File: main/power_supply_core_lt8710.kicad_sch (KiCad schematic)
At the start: 31 parts, among them Q601 IXTP28P065T, Q602 TK4R3E06PL, U601 LT8710

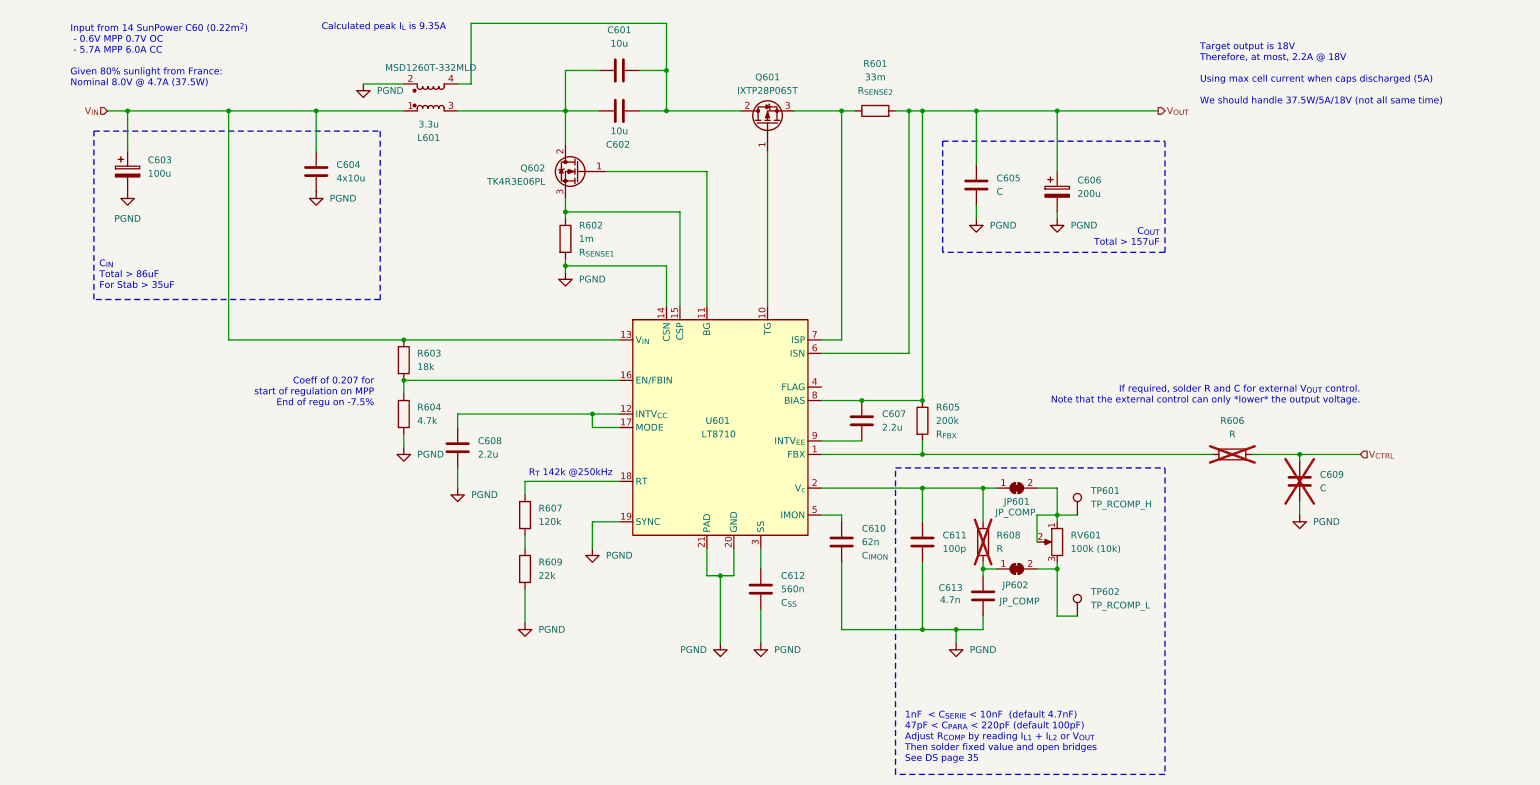
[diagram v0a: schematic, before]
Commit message: Finalize sch and start component mapping
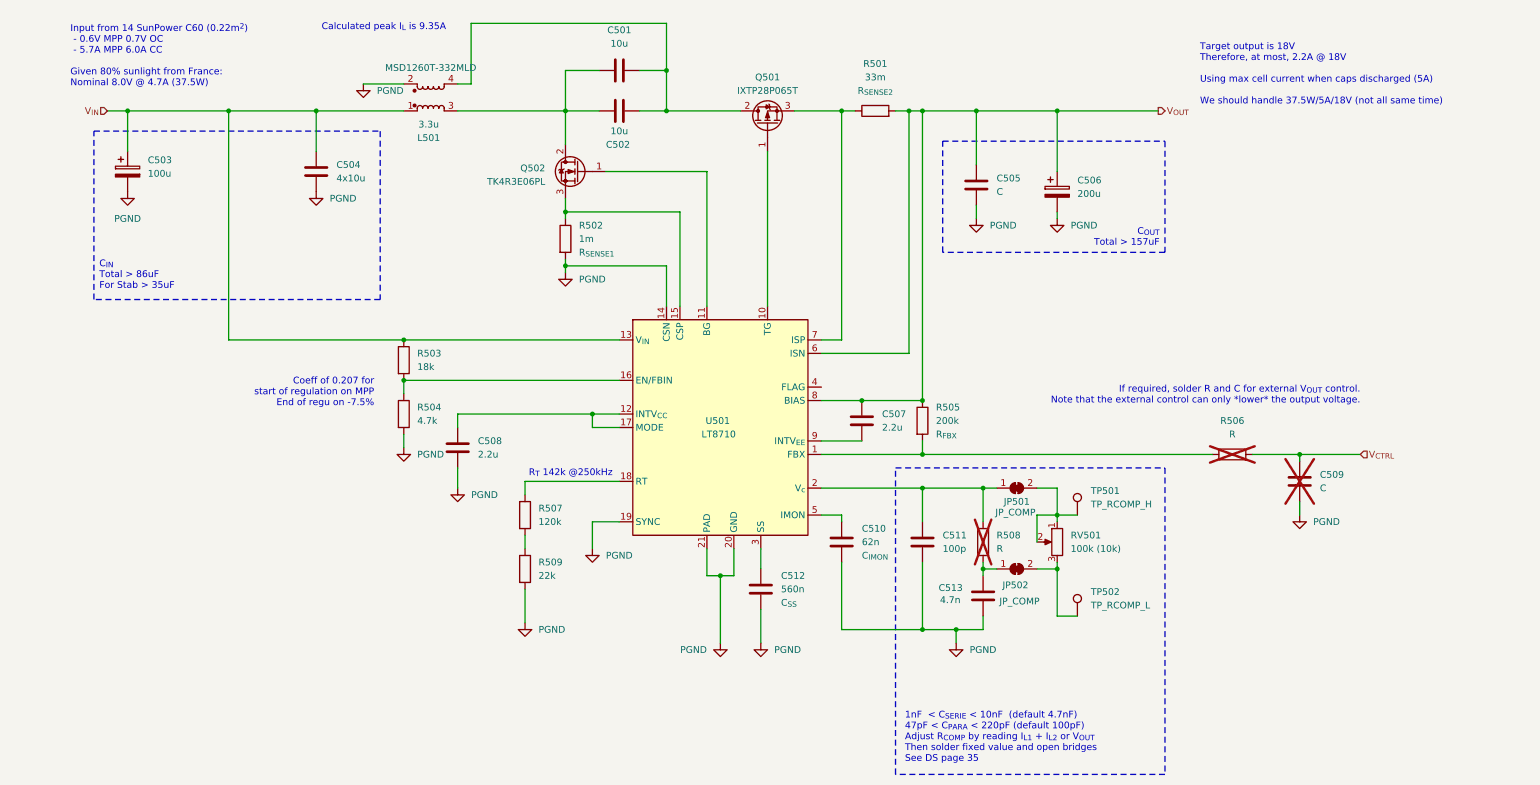
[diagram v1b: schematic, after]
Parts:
- C501: renamed from C601; footprint (none) -> Capacitor_SMD:C_0805_2012Metric
- C502: renamed from C602; footprint (none) -> Capacitor_SMD:C_0805_2012Metric
- C503: renamed from C603; footprint (none) -> Capacitor_SMD:C_0805_2012Metric
- C507: renamed from C607; footprint (none) -> Capacitor_SMD:C_0805_2012Metric
- C508: renamed from C608; footprint (none) -> Capacitor_SMD:C_0805_2012Metric
- C510: renamed from C610; footprint (none) -> Capacitor_SMD:C_0805_2012Metric
- C511: renamed from C611; footprint (none) -> Capacitor_SMD:C_0805_2012Metric
- C512: renamed from C612; footprint (none) -> Capacitor_SMD:C_0805_2012Metric
- C513: renamed from C613; footprint (none) -> Capacitor_SMD:C_0805_2012Metric
- JP501: renamed from JP601; footprint (none) -> Jumper:SolderJumper-2_P1.3mm_Open_TrianglePad1.0x1.5mm
- JP502: renamed from JP602; footprint (none) -> Jumper:SolderJumper-2_P1.3mm_Open_TrianglePad1.0x1.5mm
- Q501: renamed from Q601; footprint (none) -> Package_TO_SOT_THT:TO-220-3_Horizontal_TabUp
- R503: renamed from R603; footprint (none) -> Resistor_SMD:R_0805_2012Metric
- R504: renamed from R604; footprint (none) -> Resistor_SMD:R_0805_2012Metric
- R505: renamed from R605; footprint (none) -> Resistor_SMD:R_0805_2012Metric
- R506: renamed from R606; footprint (none) -> Resistor_SMD:R_0805_2012Metric
- R507: renamed from R607; footprint (none) -> Resistor_SMD:R_0805_2012Metric
- R508: renamed from R608; footprint (none) -> Resistor_SMD:R_0805_2012Metric
- R509: renamed from R609; footprint (none) -> Resistor_SMD:R_0805_2012Metric
- renumbered C604 to C504, C605 to C505, C606 to C506, C609 to C509, L601 to L501, Q602 to Q502, R601 to R501, R602 to R502, RV601 to RV501, TP601 to TP501, TP602 to TP502, U601 to U501

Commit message: update BOM
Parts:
- added C504, C505, C506: 10u, Capacitor_SMD:C_0805_2012Metric, symbol Device:C
- C507: renamed from C504; value 4x10u -> 10u; footprint (none) -> Capacitor_SMD:C_0805_2012Metric
- TP501, TP502: footprint (none) -> TestPoint:TestPoint_Keystone_5010-5014_Multipurpose
- renumbered C505 to C508, C506 to C509, C507 to C510, C508 to C511, C509 to C512, C510 to C513, C511 to C514, C512 to C515, C513 to C516
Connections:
- net PGND: now also C504.2, C505.2, C506.2
- net V_{IN}: now also C504.1, C505.1, C506.1
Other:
- moved on the sheet: C503, C507

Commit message: BOM OK
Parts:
- removed C508: C, symbol Device:C
- added C508: 100u, Capacitor_THT:CP_Radial_D6.3mm_P2.50mm, symbol Device:C_Polarized
- C509: value 200u -> 100u; footprint (none) -> Capacitor_THT:CP_Radial_D6.3mm_P2.50mm
- C512: footprint (none) -> Capacitor_SMD:C_0805_2012Metric
- L501: footprint (none) -> dsv4:Coilcraft_MSD1260T
- R501: footprint (none) -> Crystal:Crystal_SMD_5032-2Pin_5.0x3.2mm
- R502: footprint (none) -> Resistor_SMD:R_2010_5025Metric; MPN (none) -> WSL20101L000FEA
- RV501: footprint (none) -> Potentiometer_THT:Potentiometer_Bourns_3296W_Vertical
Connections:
- net PGND: now also C508.2
- net V_{OUT}: now also C508.1
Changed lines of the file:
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@@
-	)
-	(symbol
-		(lib_id "Device:C")
-		(at 190.5 44.45 0)
-		(unit 1)
-		(exclude_from_sim no)
-		(in_bom yes)
-		(on_board yes)
-		(dnp no)
-		(fields_autoplaced yes)
-		(property "Reference" "C508"
-			(at 194.31 43.1799 0)
-			(effects
-				(font
-					(size 1.27 1.27)
-				)
-				(justify left)
-			)
-		)
-		(property "Value" "C"
-			(at 194.31 45.7199 0)
-			(effects
-				(font
-					(size 1.27 1.27)
-				)
-				(justify left)
-			)
-		)
-		(property "Footprint" ""
-			(at 191.4652 48.26 0)
-			(effects
-				(font
-					(size 1.27 1.27)
-				)
-				(hide yes)
-			)
-		)
-		(property "Datasheet" "~"
-			(at 190.5 44.45 0)
-			(effects
-				(font
-					(size 1.27 1.27)
-				)
-				(hide yes)
-			)
-		)
-		(property "Description" "Unpolarized capacitor"
-			(at 190.5 44.45 0)
-			(effects
-				(font
-					(size 1.27 1.27)
-				)
-				(hide yes)
-			)
-		)
-		(pin "1"
-		)
-		(pin "2"
-		)
-		(instances
-			(project "dsv4"
-				(path "/c07e9297-fde8-4755-803e-d05072cd6096/164e5be8-13e0-4d66-ab9d-977f2147e774/1418bcac-62b9-409d-afe1-faaf812fdfa2"
-					(reference "C508")
-					(unit 1)
-				)
-			)
-		)
 	)
 	(symbol
@@
 			)
 		)
-		(property "Footprint" ""
+		(property "Footprint" "dsv4:Coilcraft_MSD1260T"
 			(at 87.63 27.94 0)
 			(effects
@@
 			)
 		)
-		(property "Footprint" ""
+		(property "Footprint" "Resistor_SMD:R_2010_5025Metric"
 			(at 111.252 54.61 90)
 			(effects
@@
 			)
 		)
-		(property "MPN" ""
+		(property "MPN" "WSL20101L000FEA"
 			(at 113.03 54.61 0)
 			(effects
@@
 			)
 		)
-		(property "Footprint" ""
+		(property "Footprint" "Potentiometer_THT:Potentiometer_Bourns_3296W_Vertical"
 			(at 205.74 111.76 0)
 			(effects
@@
 			)
 		)
-		(property "Footprint" ""
+		(property "Footprint" "Capacitor_SMD:C_0805_2012Metric"
 			(at 252.4252 104.14 0)
 			(effects
@@
 			)
 		)
-		(property "Footprint" ""
+		(property "Footprint" "Crystal:Crystal_SMD_5032-2Pin_5.0x3.2mm"
 			(at 171.45 32.258 90)
 			(effects
@@
 	)
 	(symbol
+		(lib_id "Device:C_Polarized")
+		(at 190.5 44.45 0)
+		(unit 1)
+		(exclude_from_sim no)
+		(in_bom yes)
+		(on_board yes)
+		(dnp no)
+		(fields_autoplaced yes)
+		(property "Reference" "C508"
+			(at 194.31 42.2909 0)
+			(effects
+				(font
+					(size 1.27 1.27)
+				)
+				(justify left)
+			)
+		)
+		(property "Value" "100u"
+			(at 194.31 44.8309 0)
+			(effects
+				(font
+					(size 1.27 1.27)
+				)
+				(justify left)
+			)
+		)
+		(property "Footprint" "Capacitor_THT:CP_Radial_D6.3mm_P2.50mm"
+			(at 191.4652 48.26 0)
+			(effects
+				(font
+					(size 1.27 1.27)
+				)
+				(hide yes)
+			)
+		)
+		(property "Datasheet" "~"
+			(at 190.5 44.45 0)
+			(effects
+				(font
+					(size 1.27 1.27)
+				)
+				(hide yes)
+			)
+		)
+		(property "Description" "Polarized capacitor"
+			(at 190.5 44.45 0)
+			(effects
+				(font
+					(size 1.27 1.27)
+				)
+				(hide yes)
+			)
+		)
+		(pin "1"
+		)
+		(pin "2"
+		)
+		(instances
+			(project "dsv4"
+				(path "/c07e9297-fde8-4755-803e-d05072cd6096/164e5be8-13e0-4d66-ab9d-977f2147e774/1418bcac-62b9-409d-afe1-faaf812fdfa2"
+					(reference "C508")
+					(unit 1)
+				)
+			)
+		)
+	)
+	(symbol
 		(lib_id "Device:R")
 		(at 82.55 77.47 0)
@@
 			)
 		)
-		(property "Value" "200u"
+		(property "Value" "100u"
 			(at 209.55 46.1009 0)
 			(effects
@@
 			)
 		)
-		(property "Footprint" ""
+		(property "Footprint" "Capacitor_THT:CP_Radial_D6.3mm_P2.50mm"
 			(at 206.7052 49.53 0)
 			(effects

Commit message: Start route PCB
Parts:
- C503: footprint Capacitor_SMD:C_0805_2012Metric -> Capacitor_THT:CP_Radial_D6.3mm_P2.50mm
- R501: footprint Crystal:Crystal_SMD_5032-2Pin_5.0x3.2mm -> Resistor_SMD:R_2010_5025Metric
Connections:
- net SW_OUT: now reaches C501.1, C502.1, L501.4, Q501.2 (D)
- net SWOUT_ISP: now reaches Q501.3 (S), R501.1, U501.7 (ISP)
- net SW_IN: now reaches C501.2, C502.2, L501.3, Q502.2 (D)
- net SWIN_CSP: now reaches Q502.3 (S), R502.1, U501.15 (CSP)
- no-connect marks 0 -> 1
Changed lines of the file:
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@@
 		(color 0 0 0 0)
 	)
+	(no_connect
+		(at 163.83 82.55)
+	)
 	(wire
 		(pts
@@
 	(wire
 		(pts
+			(xy 161.29 82.55) (xy 163.83 82.55)
+		)
+		(stroke
+			(width 0)
+			(type default)
+		)
+	)
+	(wire
+		(pts
 			(xy 191.77 128.27) (xy 191.77 125.73)
 		)
@@
 		)
 	)
+	(label "SWIN_CSP"
+		(at 116.8213 49.53 0)
+		(fields_autoplaced yes)
+		(effects
+			(font
+				(size 1.27 1.27)
+			)
+			(justify left bottom)
+		)
+	)
+	(label "SWOUT_ISP"
+		(at 165.1 49.53 90)
+		(fields_autoplaced yes)
+		(effects
+			(font
+				(size 1.27 1.27)
+			)
+			(justify left bottom)
+		)
+	)
+	(label "SW_OUT"
+		(at 99.06 13.97 0)
+		(fields_autoplaced yes)
+		(effects
+			(font
+				(size 1.27 1.27)
+			)
+			(justify left bottom)
+		)
+	)
+	(label "SW_IN"
+		(at 99.06 30.48 0)
+		(fields_autoplaced yes)
+		(effects
+			(font
+				(size 1.27 1.27)
+			)
+			(justify left bottom)
+		)
+	)
 	(hierarchical_label "V_{IN}"
 		(shape input)
@@
 			)
 		)
-		(property "Footprint" "Crystal:Crystal_SMD_5032-2Pin_5.0x3.2mm"
+		(property "Footprint" "Resistor_SMD:R_2010_5025Metric"
 			(at 171.45 32.258 90)
 			(effects
@@
 			)
 		)
-		(property "Footprint" "Capacitor_SMD:C_0805_2012Metric"
+		(property "Footprint" "Capacitor_THT:CP_Radial_D6.3mm_P2.50mm"
 			(at 21.2852 45.72 0)
 			(effects

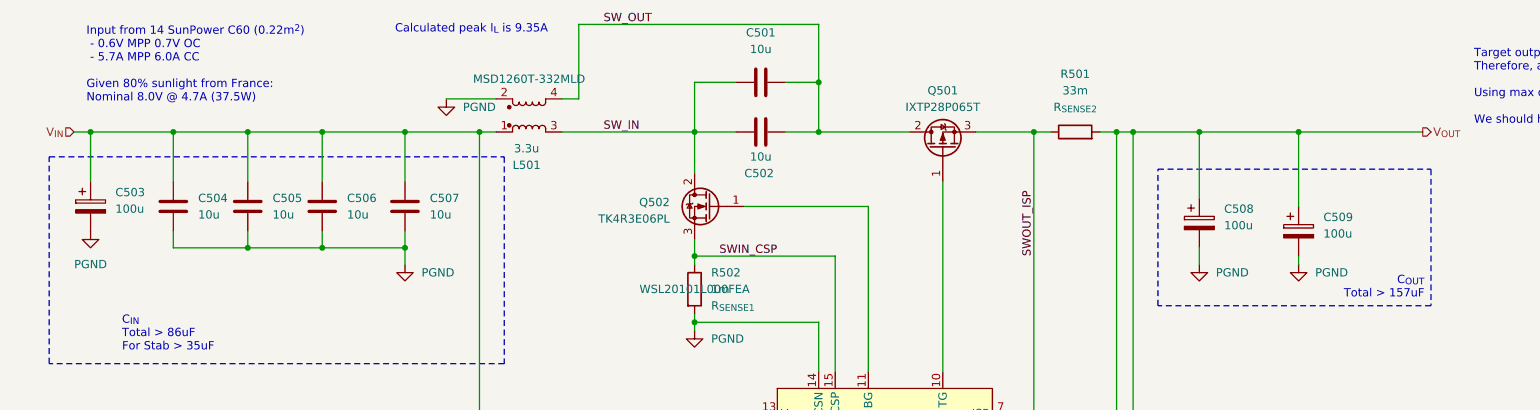
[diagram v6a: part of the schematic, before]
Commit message: Rework north route
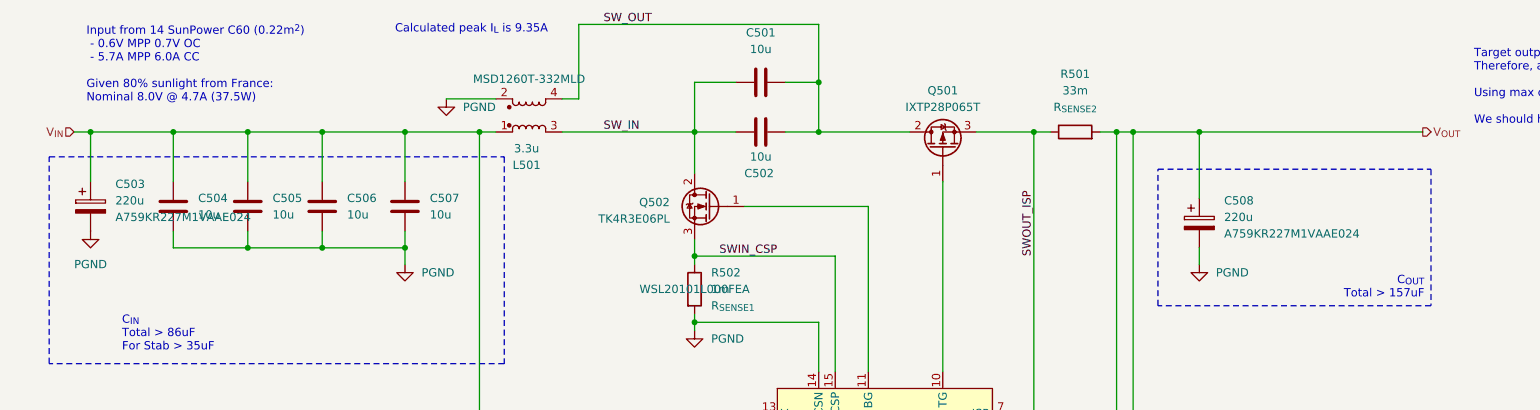
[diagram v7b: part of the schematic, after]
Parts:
- removed C509: 100u, Capacitor_THT:CP_Radial_D6.3mm_P2.50mm, symbol Device:C_Polarized
- C503, C508: value 100u -> 220u; footprint Capacitor_THT:CP_Radial_D6.3mm_P2.50mm -> Capacitor_THT:CP_Radial_D8.0mm_P3.50mm; MPN (none) -> A759KR227M1VAAE024
